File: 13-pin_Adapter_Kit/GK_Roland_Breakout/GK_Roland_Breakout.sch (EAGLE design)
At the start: 39 parts, among them T2 2N4401, U1 RC4558, U2 MIC5205-5V

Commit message: Updated BOM
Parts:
- removed H6, H8: 7P_ZIF_59453-071110EDHLF, CYCFI_Con:7P_ZIF_59453-071110EDHLF
- added LED: (no value), led:LED3MM
- added R9: 4.7k, resistor:R-EU_R0402
- C10, C11, C9: value 0.01u -> 0.01uF
- C12, C14: value 4.7u -> 4.7uF
- C13, C15: value 0.1u -> 0.1uF
- C5: value 1nf -> 1nF
- C6: value 1uf -> 1uF
- C8: value 0.47u -> 0.47uF; device resistor:C-EUC0805 -> resistor:C-EUC0603
- H1, H2: value (none) -> 7P_ZIF_59453-071110EDHLF; device con-lstb:MA04-2 -> CYCFI_Con:7P_ZIF_59453-071110EDHLF
- H7: value 7P_ZIF_59453-071110EDHLF -> (none); device CYCFI_Con:7P_ZIF_59453-071110EDHLF -> con-lstb:MA04-2
- R3, R5: value 100 -> 100R
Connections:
- removed net N$27: H3.1, H8.4
- new net N$2: LED.A, R9.2
- net +VE: now also H4.1, H7.3; no longer H2.1, H2.3, H2.5, H2.7, H6.1, H8.1
- net -VE: now also H4.3, H7.2, H7.4; no longer H2.2, H2.4, H2.6, H2.8, H6.3, H7.3, H8.3
- net 5.4V: now also H2.1, H7.5, H7.7, R9.1; no longer H1.3, H1.5, H1.7, H4.1, H5.1
- net GND: now also H1.3, H2.2, H2.3, H3.3, H5.1, H7.6, H7.8, LED.C; no longer H1.4, H1.6, H1.8, H4.3, H5.2, H5.3, H6.2, H7.2, H8.2, H8.7
- net N$10: now also H2.4, H5.2; no longer H5.4, H7.4
- net N$13: now also H5.7; no longer H7.7
- net N$18: now also H2.5, H5.3; no longer H5.5, H7.5
- net N$19: now also H3.1; no longer H3.2
- net N$20: now also H3.2; no longer H3.3
- net N$25: now also H5.5; no longer H8.6
- net N$26: now also H5.4; no longer H8.5
- net N$5: now also H1.4; no longer H6.4
- net N$6: now also H1.5; no longer H6.5
- net N$7: now also H1.6; no longer H6.6
- net N$8: now also H1.7; no longer H6.7
- net N$9: now also H5.6; no longer H7.6
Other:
- note added: "2017070401"
- note added: "GK Internal Breakout for Nexus Project by Cycfi Research is licensed under a Creative Commons Attribution-ShareAlike 4.0 International License. Copyright CYCFI Research Inc. 2013-2017"
- note added: "GK Roland Breakout"
- note added: "GK_Vol"
- note added: "NOTE: +Ve = +7V -Ve = -7V"
- note removed: "+VE"
- note removed: "-VE"
- note removed: "201722"
- note removed: "GK Roland Breakout Project by Cycfi Research is licensed under a Creative Commons Attribution-ShareAlike 4.0 International License. Copyright CYCFI Research Inc. 2013-2017"
- note removed: "Internal Breakout Board - GK"
- note removed: "MIDI Vol"
- moved on the sheet: C10, C11, C3, C5, C6, C7, H4, H5, R6, R7, R8

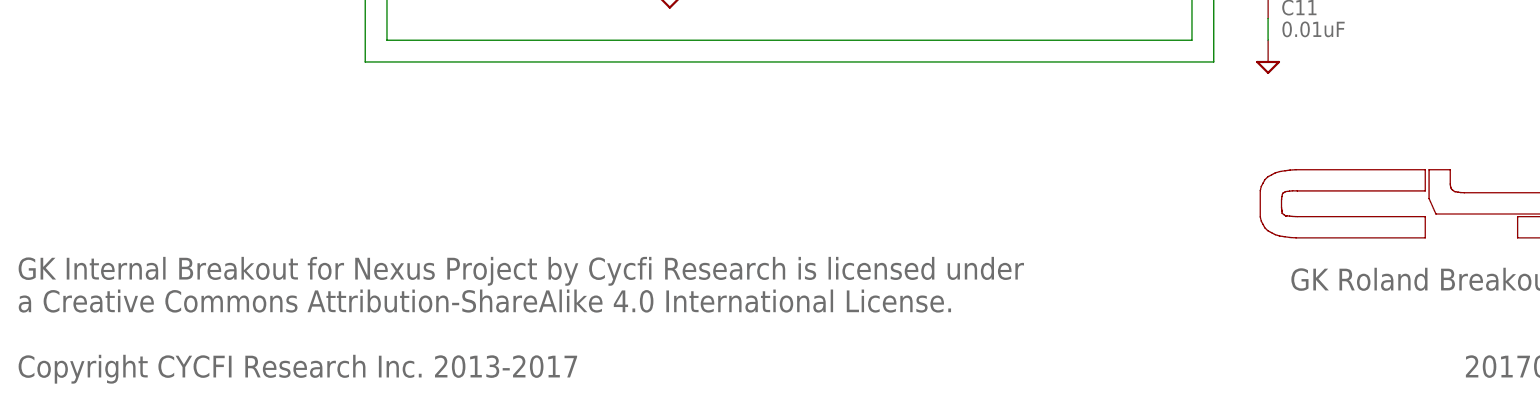
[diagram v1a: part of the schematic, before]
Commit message: Updated Notes "For Nu Project" instead of "Nexus"
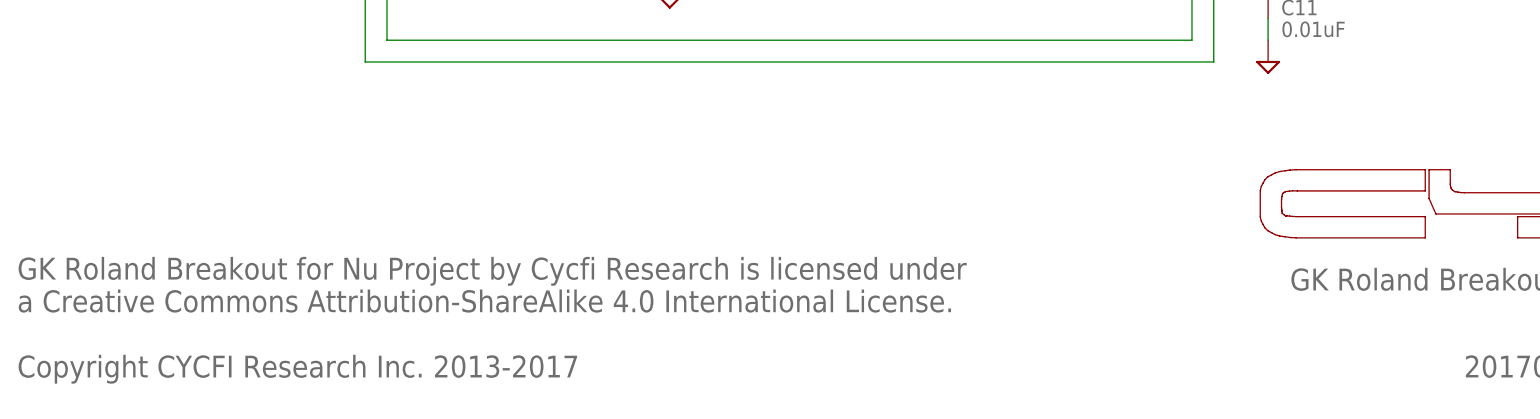
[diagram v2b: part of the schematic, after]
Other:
- note added: "GK Roland Breakout for Nu Project by Cycfi Research is licensed under a Creative Commons Attribution-ShareAlike 4.0 International License. Copyright CYCFI Research Inc. 2013-2017"
- note removed: "GK Internal Breakout for Nexus Project by Cycfi Research is licensed under a Creative Commons Attribution-ShareAlike 4.0 International License. Copyright CYCFI Research Inc. 2013-2017"
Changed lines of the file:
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@@
 <?xml version="1.0" encoding="utf-8"?>
 <!DOCTYPE eagle SYSTEM "eagle.dtd">
-<eagle version="6.3">
+<eagle version="7.6.0">
 <drawing>
 <settings>
@@
 <sheet>
 <plain>
-<text x="13.97" y="8.89" size="2.54" layer="95">GK Internal Breakout for Nexus Project by Cycfi Research is licensed under
+<text x="13.97" y="8.89" size="2.54" layer="95">GK Roland Breakout for Nu Project by Cycfi Research is licensed under
 a Creative Commons Attribution-ShareAlike 4.0 International License.
 Copyright CYCFI Research Inc. 2013-2017</text>

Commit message: Updated document number.
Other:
- note added: "2017023"
- note removed: "2017070401"
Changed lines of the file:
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@@
 <text x="33.655" y="71.755" size="1.778" layer="95" rot="R180">GND</text>
 <text x="236.22" y="7.62" size="2.54" layer="95">0.9</text>
-<text x="182.88" y="8.89" size="2.54" layer="95">2017070401</text>
+<text x="185.42" y="11.43" size="2.54" layer="95">2017023</text>
 <text x="219.71" y="46.99" size="2.54" layer="95">NOTE:
 +Ve = +7V
